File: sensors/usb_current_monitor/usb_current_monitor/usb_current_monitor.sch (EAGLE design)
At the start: 8 parts, among them J1 UJ2-AH-1-SMT-TR, U1 INA169NA/3K

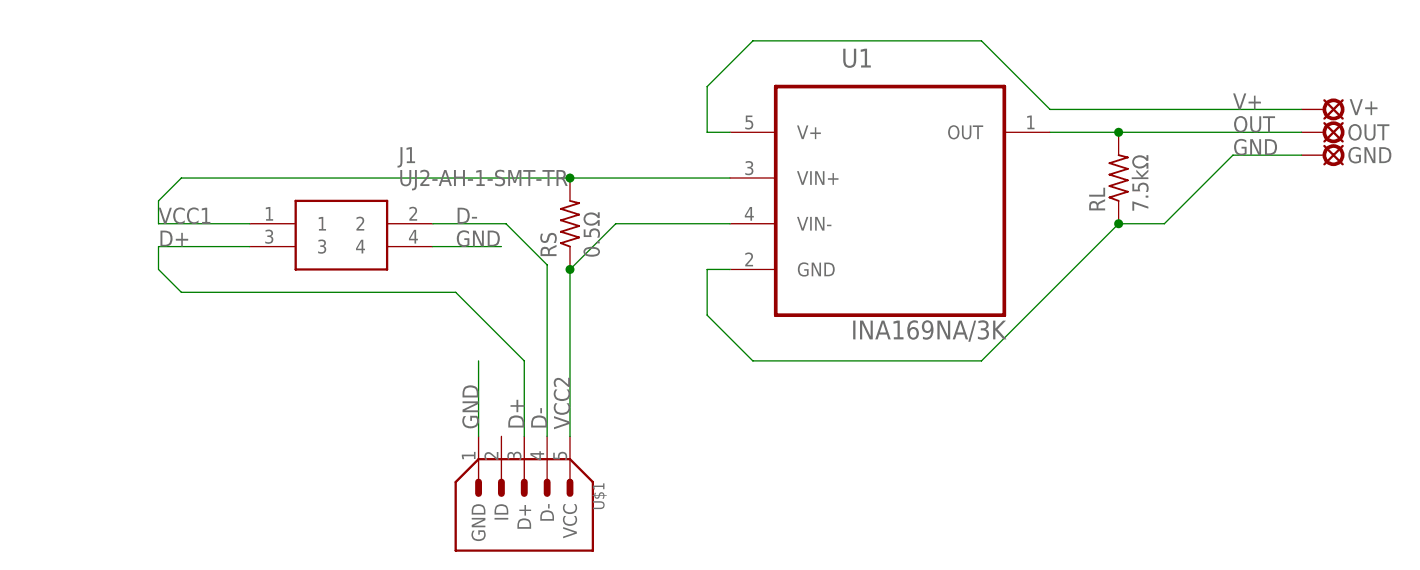
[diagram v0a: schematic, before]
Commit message: error correction on usb current monitor board
Flipped VIN+ and VIN- on the current sensor to conform with correct direction of current flow
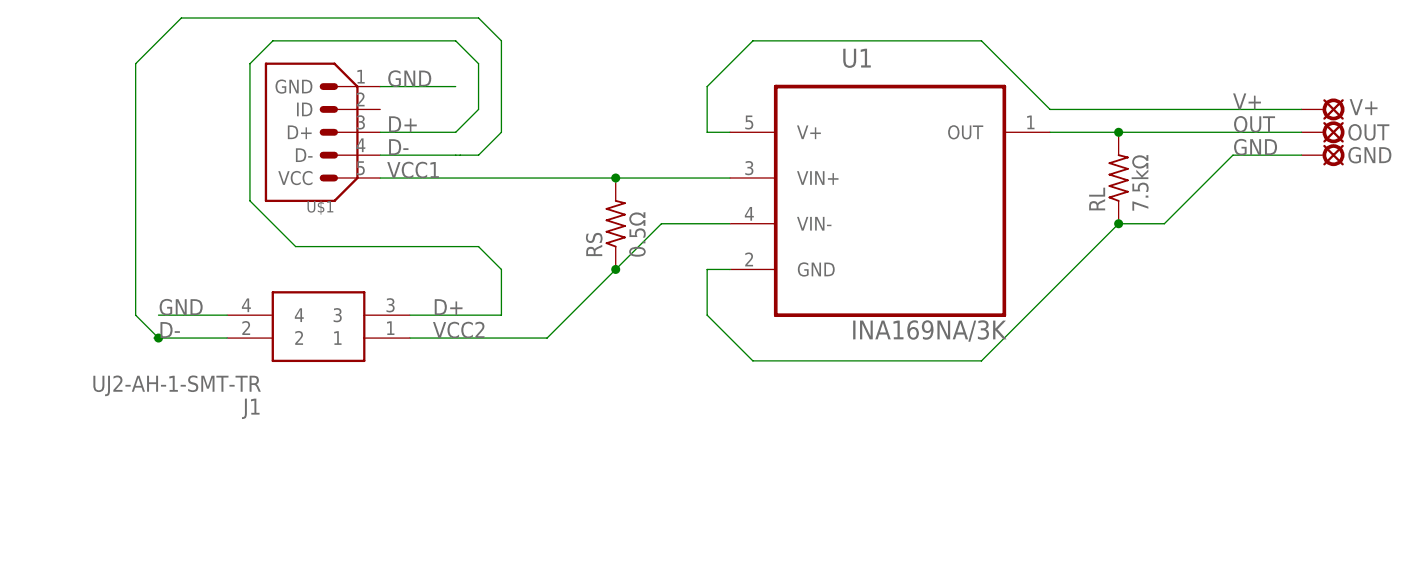
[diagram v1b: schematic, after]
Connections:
- net VCC1: now also U$1.VCC; no longer J1.1
- net VCC2: now also J1.1; no longer U$1.VCC
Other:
- moved on the sheet: J1, RS, U$1
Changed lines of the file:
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@@
 <instances>
 <instance part="U1" gate="A" x="96.52" y="60.96"/>
-<instance part="J1" gate="G$1" x="25.4" y="55.88"/>
-<instance part="U$1" gate="G$1" x="55.88" y="22.86" rot="R270"/>
+<instance part="J1" gate="G$1" x="43.18" y="43.18" rot="R180"/>
+<instance part="U$1" gate="G$1" x="30.48" y="66.04" rot="R180"/>
 <instance part="V+" gate="1" x="144.78" y="68.58" smashed="yes" rot="R270">
 <attribute name="NAME" x="147.574" y="67.945" size="1.778" layer="95"/>
@@
 <attribute name="NAME" x="147.32" y="62.611" size="1.778" layer="95"/>
 </instance>
-<instance part="RS" gate="G$1" x="60.96" y="55.88" rot="R90"/>
+<instance part="RS" gate="G$1" x="66.04" y="55.88" rot="R90"/>
 <instance part="RL" gate="G$1" x="121.92" y="60.96" rot="R90"/>
 </instances>
@@
 <net name="D-" class="0">
 <segment>
+<pinref part="J1" gate="G$1" pin="2"/>
+<wire x1="22.86" y1="43.18" x2="15.24" y2="43.18" width="0.1524" layer="91"/>
+<label x="15.24" y="43.18" size="1.778" layer="95"/>
+<wire x1="15.24" y1="43.18" x2="14.732" y2="43.18" width="0.1524" layer="91"/>
+<wire x1="15.24" y1="43.18" x2="12.7" y2="45.72" width="0.1524" layer="91"/>
+<junction x="15.24" y="43.18"/>
+<wire x1="12.7" y1="45.72" x2="12.7" y2="73.66" width="0.1524" layer="91"/>
+<wire x1="12.7" y1="73.66" x2="17.78" y2="78.74" width="0.1524" layer="91"/>
+<wire x1="17.78" y1="78.74" x2="50.8" y2="78.74" width="0.1524" layer="91"/>
+<wire x1="50.8" y1="78.74" x2="53.34" y2="76.2" width="0.1524" layer="91"/>
+<wire x1="53.34" y1="76.2" x2="53.34" y2="66.04" width="0.1524" layer="91"/>
+<wire x1="53.34" y1="66.04" x2="50.8" y2="63.5" width="0.1524" layer="91"/>
 <pinref part="U$1" gate="G$1" pin="D-"/>
-<label x="58.42" y="33.02" size="1.778" layer="95" rot="R90"/>
-<pinref part="J1" gate="G$1" pin="2"/>
-<wire x1="45.72" y1="55.88" x2="53.848" y2="55.88" width="0.1524" layer="91"/>
-<label x="48.26" y="55.88" size="1.778" layer="95"/>
-<wire x1="58.42" y1="32.258" x2="58.42" y2="51.308" width="0.1524" layer="91"/>
-<wire x1="58.42" y1="51.308" x2="53.848" y2="55.88" width="0.1524" layer="91"/>
+<label x="40.64" y="63.5" size="1.778" layer="95"/>
+<wire x1="39.878" y1="63.5" x2="48.26" y2="63.5" width="0.1524" layer="91"/>
+<wire x1="48.26" y1="63.5" x2="48.768" y2="63.5" width="0.1524" layer="91"/>
+<wire x1="50.8" y1="63.5" x2="48.768" y2="63.5" width="0.1524" layer="91"/>
 </segment>
 </net>
@@
 <segment>
 <pinref part="J1" gate="G$1" pin="4"/>
-<wire x1="45.72" y1="53.34" x2="53.34" y2="53.34" width="0.1524" layer="91"/>
-<label x="48.26" y="53.34" size="1.778" layer="95"/>
+<wire x1="22.86" y1="45.72" x2="15.24" y2="45.72" width="0.1524" layer="91"/>
+<label x="15.24" y="45.72" size="1.778" layer="95"/>
 </segment>
 <segment>
 <pinref part="U$1" gate="G$1" pin="GND"/>
-<wire x1="50.8" y1="32.258" x2="50.8" y2="40.64" width="0.1524" layer="91"/>
-<label x="50.8" y="33.02" size="1.778" layer="95" rot="R90"/>
+<wire x1="39.878" y1="71.12" x2="48.26" y2="71.12" width="0.1524" layer="91"/>
+<label x="40.64" y="71.12" size="1.778" layer="95"/>
 </segment>
 <segment>
@@
 </segment>
 </net>
-<net name="VCC1" class="0">
+<net name="VCC2" class="0">
 <segment>
+<pinref part="U1" gate="A" pin="VIN-"/>
+<pinref part="RS" gate="G$1" pin="1"/>
+<wire x1="78.74" y1="55.88" x2="71.12" y2="55.88" width="0.1524" layer="91"/>
+<wire x1="71.12" y1="55.88" x2="66.04" y2="50.8" width="0.1524" layer="91"/>
 <pinref part="J1" gate="G$1" pin="1"/>
-<wire x1="25.4" y1="55.88" x2="15.24" y2="55.88" width="0.1524" layer="91"/>
-<label x="15.24" y="55.88" size="1.778" layer="95"/>
-<pinref part="U1" gate="A" pin="VIN+"/>
-<wire x1="78.74" y1="60.96" x2="60.96" y2="60.96" width="0.1524" layer="91"/>
-<wire x1="60.96" y1="60.96" x2="17.78" y2="60.96" width="0.1524" layer="91"/>
-<wire x1="17.78" y1="60.96" x2="15.24" y2="58.42" width="0.1524" layer="91"/>
-<wire x1="15.24" y1="58.42" x2="15.24" y2="55.88" width="0.1524" layer="91"/>
-<pinref part="RS" gate="G$1" pin="2"/>
-<junction x="60.96" y="60.96"/>
+<wire x1="43.18" y1="43.18" x2="58.42" y2="43.18" width="0.1524" layer="91"/>
+<label x="45.72" y="43.18" size="1.778" layer="95"/>
+<wire x1="66.04" y1="50.8" x2="58.42" y2="43.18" width="0.1524" layer="91"/>
+<junction x="66.04" y="50.8"/>
 </segment>
 </net>
@@
 <segment>
 <pinref part="U$1" gate="G$1" pin="D+"/>
-<wire x1="55.88" y1="32.258" x2="55.88" y2="40.64" width="0.1524" layer="91"/>
-<label x="55.88" y="33.02" size="1.778" layer="95" rot="R90"/>
-<wire x1="55.88" y1="40.64" x2="48.26" y2="48.26" width="0.1524" layer="91"/>
-<wire x1="48.26" y1="48.26" x2="17.78" y2="48.26" width="0.1524" layer="91"/>
+<wire x1="39.878" y1="66.04" x2="48.26" y2="66.04" width="0.1524" layer="91"/>
+<label x="40.64" y="66.04" size="1.778" layer="95"/>
+<wire x1="48.26" y1="66.04" x2="50.8" y2="68.58" width="0.1524" layer="91"/>
+<wire x1="50.8" y1="68.58" x2="50.8" y2="73.66" width="0.1524" layer="91"/>
+<wire x1="50.8" y1="73.66" x2="48.26" y2="76.2" width="0.1524" layer="91"/>
+<wire x1="48.26" y1="76.2" x2="27.94" y2="76.2" width="0.1524" layer="91"/>
+<wire x1="27.94" y1="76.2" x2="25.4" y2="73.66" width="0.1524" layer="91"/>
+<wire x1="25.4" y1="73.66" x2="25.4" y2="58.42" width="0.1524" layer="91"/>
+<wire x1="25.4" y1="58.42" x2="30.48" y2="53.34" width="0.1524" layer="91"/>
+<wire x1="30.48" y1="53.34" x2="50.8" y2="53.34" width="0.1524" layer="91"/>
+<wire x1="50.8" y1="53.34" x2="53.34" y2="50.8" width="0.1524" layer="91"/>
 <pinref part="J1" gate="G$1" pin="3"/>
-<wire x1="25.4" y1="53.34" x2="15.24" y2="53.34" width="0.1524" layer="91"/>
-<label x="15.24" y="53.34" size="1.778" layer="95"/>
-<wire x1="17.78" y1="48.26" x2="15.24" y2="50.8" width="0.1524" layer="91"/>
-<wire x1="15.24" y1="50.8" x2="15.24" y2="53.34" width="0.1524" layer="91"/>
+<wire x1="43.18" y1="45.72" x2="53.34" y2="45.72" width="0.1524" layer="91"/>
+<label x="45.72" y="45.72" size="1.778" layer="95"/>
+<wire x1="53.34" y1="50.8" x2="53.34" y2="45.72" width="0.1524" layer="91"/>
 </segment>
 </net>
-<net name="VCC2" class="0">
+<net name="VCC1" class="0">
 <segment>
 <pinref part="U$1" gate="G$1" pin="VCC"/>
-<wire x1="60.96" y1="32.258" x2="60.96" y2="50.8" width="0.1524" layer="91"/>
-<label x="60.96" y="33.02" size="1.778" layer="95" rot="R90"/>
-<pinref part="RS" gate="G$1" pin="1"/>
-<pinref part="U1" gate="A" pin="VIN-"/>
-<wire x1="78.74" y1="55.88" x2="66.04" y2="55.88" width="0.1524" layer="91"/>
-<wire x1="60.96" y1="50.8" x2="66.04" y2="55.88" width="0.1524" layer="91"/>
-<junction x="60.96" y="50.8"/>
+<label x="40.64" y="60.96" size="1.778" layer="95"/>
+<pinref part="U1" gate="A" pin="VIN+"/>
+<wire x1="78.74" y1="60.96" x2="66.04" y2="60.96" width="0.1524" layer="91"/>
+<pinref part="RS" gate="G$1" pin="2"/>
+<wire x1="66.04" y1="60.96" x2="39.878" y2="60.96" width="0.1524" layer="91"/>
+<junction x="66.04" y="60.96"/>
 </segment>
 </net>
@@
 </sheet>
 </sheets>
+<errors>
+</errors>
 </schematic>
 </drawing>
